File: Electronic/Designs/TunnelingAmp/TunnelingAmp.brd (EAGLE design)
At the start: 35 x 25 mm, 8 parts, among them U1 OPA627AUE4

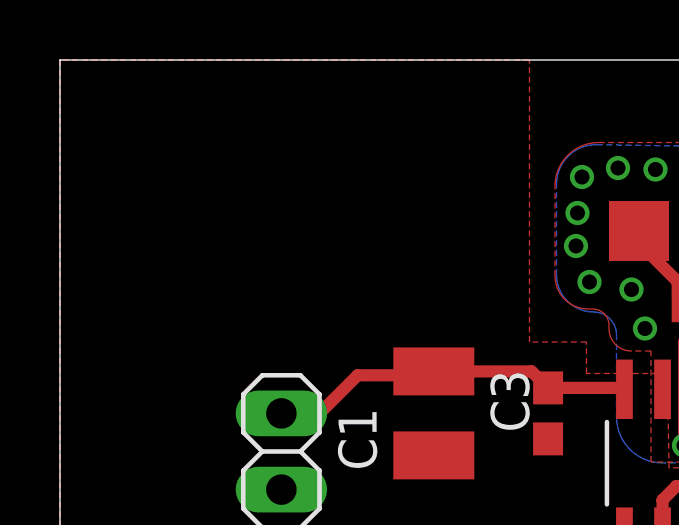
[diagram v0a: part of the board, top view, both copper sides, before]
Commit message: Added better Cmake QT Find and added dac2 piezo and tun boards
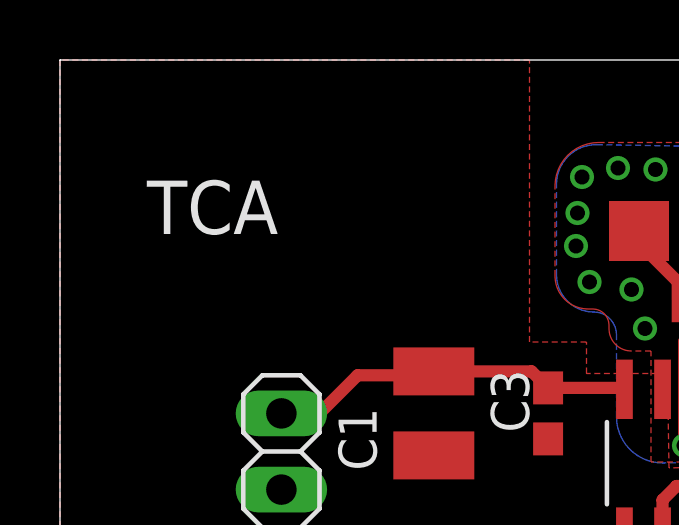
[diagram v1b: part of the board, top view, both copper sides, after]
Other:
- board text added: "TCA"
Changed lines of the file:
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@@
 <vertex x="16.15" y="25"/>
 </polygon>
+<text x="2.9" y="19.2" size="1.778" layer="21">TCA</text>
 </plain>
 <attributes>
